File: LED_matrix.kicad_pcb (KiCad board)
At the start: 2 copper layers, 26 x 52 mm, 77 parts, among them J1 Conn_02x20_Odd_Even

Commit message: start adding more dense LED matrix
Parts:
- added D61: LED, custom_LED_footprint:LED_0402_1005Metric, F.Cu at (125.0, 87.9)
- added D62: LED, custom_LED_footprint:LED_0402_1005Metric, F.Cu at (124.9, 89.1)
- added D63: LED, custom_LED_footprint:LED_0402_1005Metric, F.Cu at (125.1, 91.2)
- added D64: LED, custom_LED_footprint:LED_0402_1005Metric, F.Cu at (127.5, 90.8)
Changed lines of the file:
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@@
     (tracks 426)
     (zones 0)
-    (modules 77)
-    (nets 33)
+    (modules 81)
+    (nets 37)
   )
   (page A4)
@@
   (net 31 /c_4)
   (net 32 /c_5)
+  (net 33 "Net-(D61-Pad1)")
+  (net 34 "Net-(D61-Pad2)")
+  (net 35 "Net-(D62-Pad2)")
+  (net 36 "Net-(D63-Pad1)")
   (net_class Default "This is the default net class."
     (clearance 0.18)
@@
     (add_net /row_8)
     (add_net /row_9)
+    (add_net "Net-(D61-Pad1)")
+    (add_net "Net-(D61-Pad2)")
+    (add_net "Net-(D62-Pad2)")
+    (add_net "Net-(D63-Pad1)")
   )
   (module Connector_PinHeader_2.54mm:PinHeader_2x20_P2.54mm_Vertical (layer B.Cu)
@@
     (model ${KISYS3DMOD}/LED_SMD.3dshapes/LED_0402_1005Metric.wrl
       (at (xyz 0 0 0))
+      (scale (xyz 1 1 1))
+      (rotate (xyz 0 0 0))
+    )
+  )
+  (module custom_LED_footprint:LED_0402_1005Metric (layer F.Cu)
+    (at 125 87.9 135)
+    (descr "LED SMD 0402 (1005 Metric), square (rectangular) end terminal, IPC_7351 nominal, (Body size source: http://www.tortai-tech.com/upload/download/2011102023233369053.pdf), generated with kicad-footprint-generator")
+    (tags LED)
+    (attr smd)
+    (fp_text reference D61 (at 0 -1.17 135) (layer F.SilkS)
+      (effects (font (size 1 1) (thickness 0.15)))
+    )
+    (fp_text value LED (at 0 1.17 135) (layer F.Fab)
+      (effects (font (size 1 1) (thickness 0.15)))
+    )
+    (fp_circle (center -1.09 0) (end -1.04 0) (layer F.SilkS) (width 0.1))
+    (fp_line (start -0.5 0.25) (end -0.5 -0.25) (layer F.Fab) (width 0.1))
+    (fp_line (start -0.5 -0.25) (end 0.5 -0.25) (layer F.Fab) (width 0.1))
+    (fp_line (start 0.5 -0.25) (end 0.5 0.25) (layer F.Fab) (width 0.1))
+    (fp_line (start 0.5 0.25) (end -0.5 0.25) (layer F.Fab) (width 0.1))
+    (fp_line (start -0.4 0.25) (end -0.4 -0.25) (layer F.Fab) (width 0.1))
+    (fp_line (start -0.3 0.25) (end -0.3 -0.25) (layer F.Fab) (width 0.1))
+    (fp_line (start -0.93 0.47) (end -0.93 -0.47) (layer F.CrtYd) (width 0.05))
+    (fp_line (start -0.93 -0.47) (end 0.93 -0.47) (layer F.CrtYd) (width 0.05))
+    (fp_line (start 0.93 -0.47) (end 0.93 0.47) (layer F.CrtYd) (width 0.05))
+    (fp_line (start 0.93 0.47) (end -0.93 0.47) (layer F.CrtYd) (width 0.05))
+    (fp_text user %R (at 0 0 135) (layer F.Fab)
+      (effects (font (size 0.25 0.25) (thickness 0.04)))
+    )
+    (pad 1 smd rect (at -0.4 0 135) (size 0.6 0.5) (layers F.Cu F.Paste F.Mask)
+      (net 33 "Net-(D61-Pad1)"))
+    (pad 2 smd rect (at 0.4 0 135) (size 0.6 0.5) (layers F.Cu F.Paste F.Mask)
+      (net 34 "Net-(D61-Pad2)"))
+    (model ${KISYS3DMOD}/LED_SMD.3dshapes/LED_0402_1005Metric.wrl
+      (at (xyz 0 0 0))
+      (scale (xyz 1 1 1))
+      (rotate (xyz 0 0 0))
+    )
+  )
+  (module custom_LED_footprint:LED_0402_1005Metric (layer F.Cu)
+    (at 124.925 89.1 315)
+    (descr "LED SMD 0402 (1005 Metric), square (rectangular) end terminal, IPC_7351 nominal, (Body size source: http://www.tortai-tech.com/upload/download/2011102023233369053.pdf), generated with kicad-footprint-generator")
+    (tags LED)
+    (attr smd)
+    (fp_text reference D62 (at 0 -1.17 315) (layer F.SilkS)
+      (effects (font (size 1 1) (thickness 0.15)))
+    )
+    (fp_text value LED (at 0 1.17 315) (layer F.Fab)
+      (effects (font (size 1 1) (thickness 0.15)))
+    )
+    (fp_circle (center -1.09 0) (end -1.04 0) (layer F.SilkS) (width 0.1))
+    (fp_line (start -0.5 0.25) (end -0.5 -0.25) (layer F.Fab) (width 0.1))
+    (fp_line (start -0.5 -0.25) (end 0.5 -0.25) (layer F.Fab) (width 0.1))
+    (fp_line (start 0.5 -0.25) (end 0.5 0.25) (layer F.Fab) (width 0.1))
+    (fp_line (start 0.5 0.25) (end -0.5 0.25) (layer F.Fab) (width 0.1))
+    (fp_line (start -0.4 0.25) (end -0.4 -0.25) (layer F.Fab) (width 0.1))
+    (fp_line (start -0.3 0.25) (end -0.3 -0.25) (layer F.Fab) (width 0.1))
+    (fp_line (start -0.93 0.47) (end -0.93 -0.47) (layer F.CrtYd) (width 0.05))
+    (fp_line (start -0.93 -0.47) (end 0.93 -0.47) (layer F.CrtYd) (width 0.05))
+    (fp_line (start 0.93 -0.47) (end 0.93 0.47) (layer F.CrtYd) (width 0.05))
+    (fp_line (start 0.93 0.47) (end -0.93 0.47) (layer F.CrtYd) (width 0.05))
+    (fp_text user %R (at 0 0 315) (layer F.Fab)
+      (effects (font (size 0.25 0.25) (thickness 0.04)))
+    )
+    (pad 1 smd rect (at -0.4 0 315) (size 0.6 0.5) (layers F.Cu F.Paste F.Mask)
+      (net 33 "Net-(D61-Pad1)"))
+    (pad 2 smd rect (at 0.4 0 315) (size 0.6 0.5) (layers F.Cu F.Paste F.Mask)
+      (net 35 "Net-(D62-Pad2)"))
+    (model ${KISYS3DMOD}/LED_SMD.3dshapes/LED_0402_1005Metric.wrl
+      (at (xyz 0 0 0))
+      (scale (xyz 1 1 1))
+      (rotate (xyz 0 0 0))
+    )
+  )
+  (module custom_LED_footprint:LED_0402_1005Metric (layer F.Cu)
+    (at 125.1 91.175 135)
+    (descr "LED SMD 0402 (1005 Metric), square (rectangular) end terminal, IPC_7351 nominal, (Body size source: http://www.tortai-tech.com/upload/download/2011102023233369053.pdf), generated with kicad-footprint-generator")
+    (tags LED)
+    (attr smd)
+    (fp_text reference D63 (at 0 -1.17 135) (layer F.SilkS)
+      (effects (font (size 1 1) (thickness 0.15)))
+    )
+    (fp_text value LED (at 0 1.17 135) (layer F.Fab)
+      (effects (font (size 1 1) (thickness 0.15)))
+    )
+    (fp_text user %R (at 0 0 135) (layer F.Fab)
+      (effects (font (size 0.25 0.25) (thickness 0.04)))
+    )
+    (fp_line (start 0.93 0.47) (end -0.93 0.47) (layer F.CrtYd) (width 0.05))
+    (fp_line (start 0.93 -0.47) (end 0.93 0.47) (layer F.CrtYd) (width 0.05))
+    (fp_line (start -0.93 -0.47) (end 0.93 -0.47) (layer F.CrtYd) (width 0.05))
+    (fp_line (start -0.93 0.47) (end -0.93 -0.47) (layer F.CrtYd) (width 0.05))
+    (fp_line (start -0.3 0.25) (end -0.3 -0.25) (layer F.Fab) (width 0.1))
+    (fp_line (start -0.4 0.25) (end -0.4 -0.25) (layer F.Fab) (width 0.1))
+    (fp_line (start 0.5 0.25) (end -0.5 0.25) (layer F.Fab) (width 0.1))
+    (fp_line (start 0.5 -0.25) (end 0.5 0.25) (layer F.Fab) (width 0.1))
+    (fp_line (start -0.5 -0.25) (end 0.5 -0.25) (layer F.Fab) (width 0.1))
+    (fp_line (start -0.5 0.25) (end -0.5 -0.25) (layer F.Fab) (width 0.1))
+    (fp_circle (center -1.09 0) (end -1.04 0) (layer F.SilkS) (width 0.1))
+    (pad 2 smd rect (at 0.4 0 135) (size 0.6 0.5) (layers F.Cu F.Paste F.Mask)
+      (net 34 "Net-(D61-Pad2)"))
+    (pad 1 smd rect (at -0.4 0 135) (size 0.6 0.5) (layers F.Cu F.Paste F.Mask)
+      (net 36 "Net-(D63-Pad1)"))
+    (model ${KISYS3DMOD}/LED_SMD.3dshapes/LED_0402_1005Metric.wrl
+      (at (xyz 0 0 0))
+      (scale (xyz 1 1 1))
+      (rotate (xyz 0 0 0))
+    )
+  )
+  (module custom_LED_footprint:LED_0402_1005Metric (layer F.Cu)
+    (at 127.525 90.85 135)
+    (descr "LED SMD 0402 (1005 Metric), square (rectangular) end terminal, IPC_7351 nominal, (Body size source: http://www.tortai-tech.com/upload/download/2011102023233369053.pdf), generated with kicad-footprint-generator")
+    (tags LED)
+    (attr smd)
+    (fp_text reference D64 (at 0 -1.17 135) (layer F.SilkS)
+      (effects (font (size 1 1) (thickness 0.15)))
+    )
+    (fp_text value LED (at 0 1.17 135) (layer F.Fab)
+      (effects (font (size 1 1) (thickness 0.15)))
+    )
+    (fp_text user %R (at 0 0 135) (layer F.Fab)
+      (effects (font (size 0.25 0.25) (thickness 0.04)))
+    )
+    (fp_line (start 0.93 0.47) (end -0.93 0.47) (layer F.CrtYd) (width 0.05))
+    (fp_line (start 0.93 -0.47) (end 0.93 0.47) (layer F.CrtYd) (width 0.05))
+    (fp_line (start -0.93 -0.47) (end 0.93 -0.47) (layer F.CrtYd) (width 0.05))
+    (fp_line (start -0.93 0.47) (end -0.93 -0.47) (layer F.CrtYd) (width 0.05))
+    (fp_line (start -0.3 0.25) (end -0.3 -0.25) (layer F.Fab) (width 0.1))
+    (fp_line (start -0.4 0.25) (end -0.4 -0.25) (layer F.Fab) (width 0.1))
+    (fp_line (start 0.5 0.25) (end -0.5 0.25) (layer F.Fab) (width 0.1))
+    (fp_line (start 0.5 -0.25) (end 0.5 0.25) (layer F.Fab) (width 0.1))
+    (fp_line (start -0.5 -0.25) (end 0.5 -0.25) (layer F.Fab) (width 0.1))
+    (fp_line (start -0.5 0.25) (end -0.5 -0.25) (layer F.Fab) (width 0.1))
+    (fp_circle (center -1.089999 0) (end -1.04 0) (layer F.SilkS) (width 0.1))
+    (pad 2 smd rect (at 0.4 0 135) (size 0.6 0.5) (layers F.Cu F.Paste F.Mask)
+      (net 35 "Net-(D62-Pad2)"))
+    (pad 1 smd rect (at -0.4 0 135) (size 0.6 0.5) (layers F.Cu F.Paste F.Mask)
+      (net 36 "Net-(D63-Pad1)"))
+    (model ${KISYS3DMOD}/LED_SMD.3dshapes/LED_0402_1005Metric.wrl
+      (at (xyz 0 0 0))

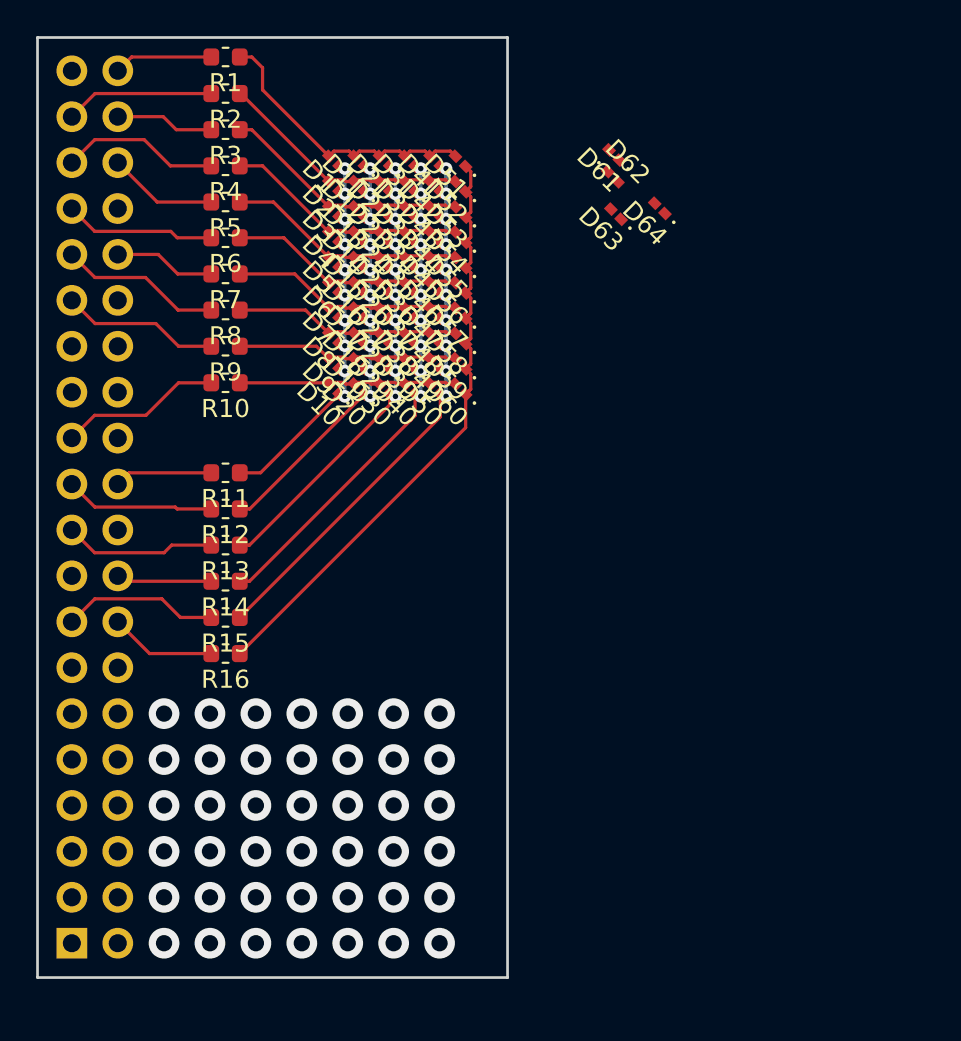
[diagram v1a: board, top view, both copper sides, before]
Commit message: add LED matrix with 1.2mm pitch
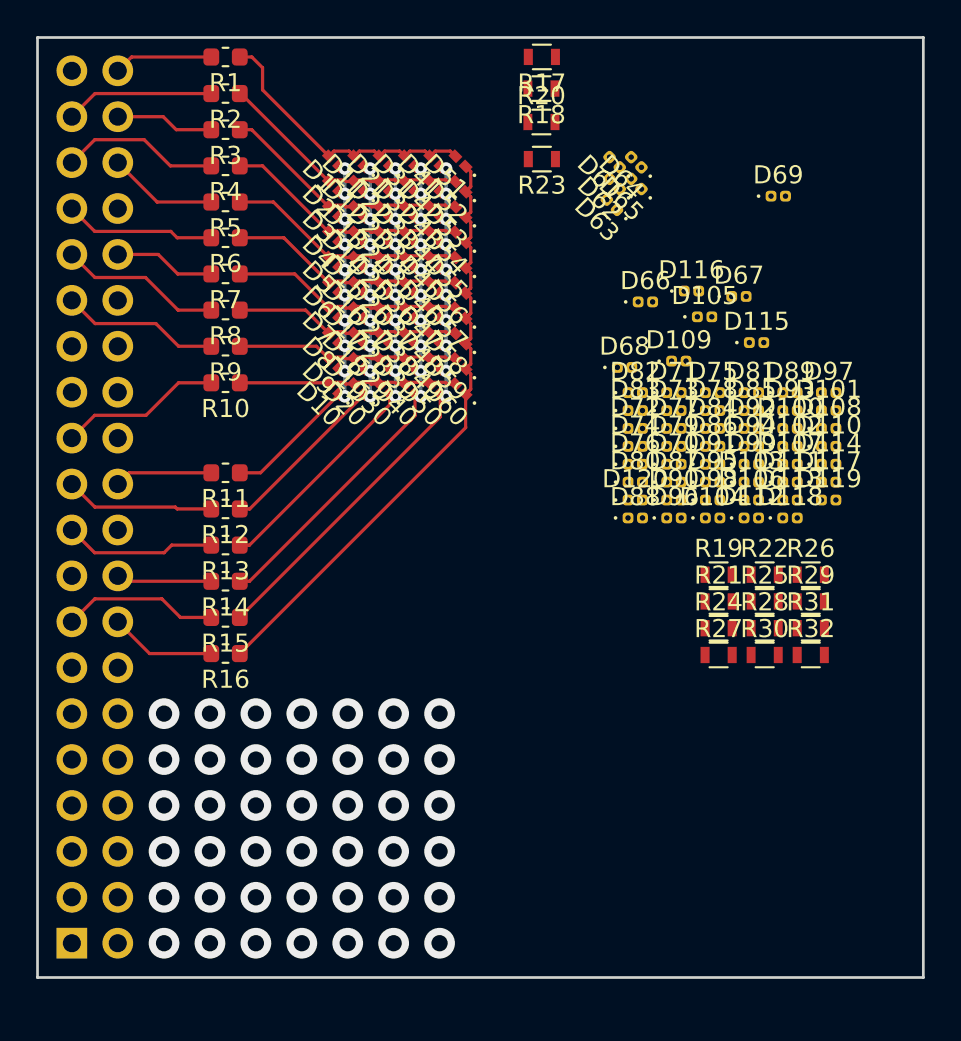
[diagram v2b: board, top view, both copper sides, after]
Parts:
- added D100: LED, custom_LED_footprint:LED_0402_round, F.Cu at (134.7, 103.0)
- added D101: LED, custom_LED_footprint:LED_0402_round, F.Cu at (136.9, 102.0)
- added D102: LED, custom_LED_footprint:LED_0402_round, F.Cu at (134.7, 104.0)
- added D103: LED, custom_LED_footprint:LED_0402_round, F.Cu at (132.6, 106.0)
- added D104: LED, custom_LED_footprint:LED_0402_round, F.Cu at (130.4, 108.0)
- added D105: LED, custom_LED_footprint:LED_0402_round, F.Cu at (130.0, 96.8)
- added D106: LED, custom_LED_footprint:LED_0402_round, F.Cu at (132.6, 107.0)
- added D107: LED, custom_LED_footprint:LED_0402_round, F.Cu at (134.7, 105.0)
- added D108: LED, custom_LED_footprint:LED_0402_round, F.Cu at (136.9, 103.0)
- added D109: LED, custom_LED_footprint:LED_0402_round, F.Cu at (128.6, 99.3)
- added D110: LED, custom_LED_footprint:LED_0402_round, F.Cu at (136.9, 104.0)
- added D111: LED, custom_LED_footprint:LED_0402_round, F.Cu at (134.7, 106.0)
- added D112: LED, custom_LED_footprint:LED_0402_round, F.Cu at (132.6, 108.0)
- added D113: LED, custom_LED_footprint:LED_0402_round, F.Cu at (134.7, 107.0)
- added D114: LED, custom_LED_footprint:LED_0402_round, F.Cu at (136.9, 105.0)
- added D115: LED, custom_LED_footprint:LED_0402_round, F.Cu at (132.9, 98.3)
- added D116: LED, custom_LED_footprint:LED_0402_round, F.Cu at (129.3, 95.4)
- added D117: LED, custom_LED_footprint:LED_0402_round, F.Cu at (136.9, 106.0)
- added D118: LED, custom_LED_footprint:LED_0402_round, F.Cu at (134.7, 108.0)
- added D119: LED, custom_LED_footprint:LED_0402_round, F.Cu at (136.9, 107.0)
- added D120: LED, custom_LED_footprint:LED_0402_round, F.Cu at (126.2, 107.0)
- added D65: LED, custom_LED_footprint:LED_0402_round, F.Cu at (126.2, 89.5)
- added D66: LED, custom_LED_footprint:LED_0402_round, F.Cu at (126.7, 96.0)
- added D67: LED, custom_LED_footprint:LED_0402_round, F.Cu at (131.9, 95.7)
- added D68: LED, custom_LED_footprint:LED_0402_round, F.Cu at (125.6, 99.7)
- added D69: LED, custom_LED_footprint:LED_0402_round, F.Cu at (134.1, 90.2)
- added D70: LED, custom_LED_footprint:LED_0402_round, F.Cu at (128.3, 105.0)
- added D71: LED, custom_LED_footprint:LED_0402_round, F.Cu at (128.3, 101.0)
- added D72: LED, custom_LED_footprint:LED_0402_round, F.Cu at (126.2, 103.0)
- added D73: LED, custom_LED_footprint:LED_0402_round, F.Cu at (128.3, 102.0)
- added D74: LED, custom_LED_footprint:LED_0402_round, F.Cu at (126.2, 104.0)
- added D75: LED, custom_LED_footprint:LED_0402_round, F.Cu at (130.4, 101.0)
- added D76: LED, custom_LED_footprint:LED_0402_round, F.Cu at (126.2, 105.0)
- added D77: LED, custom_LED_footprint:LED_0402_round, F.Cu at (128.3, 103.0)
- added D78: LED, custom_LED_footprint:LED_0402_round, F.Cu at (130.4, 102.0)
- added D79: LED, custom_LED_footprint:LED_0402_round, F.Cu at (128.3, 104.0)
- added D80: LED, custom_LED_footprint:LED_0402_round, F.Cu at (126.2, 106.0)
- added D81: LED, custom_LED_footprint:LED_0402_round, F.Cu at (132.6, 101.0)
- added D82: LED, custom_LED_footprint:LED_0402_round, F.Cu at (126.2, 101.0)
- added D83: LED, custom_LED_footprint:LED_0402_round, F.Cu at (126.2, 102.0)
- added D84: LED, custom_LED_footprint:LED_0402_round, F.Cu at (130.4, 103.0)
- added D85: LED, custom_LED_footprint:LED_0402_round, F.Cu at (132.6, 102.0)
- added D86: LED, custom_LED_footprint:LED_0402_round, F.Cu at (130.4, 104.0)
- added D87: LED, custom_LED_footprint:LED_0402_round, F.Cu at (128.3, 106.0)
- added D88: LED, custom_LED_footprint:LED_0402_round, F.Cu at (126.2, 108.0)
- added D89: LED, custom_LED_footprint:LED_0402_round, F.Cu at (134.7, 101.0)
- added D90: LED, custom_LED_footprint:LED_0402_round, F.Cu at (128.3, 107.0)
- added D91: LED, custom_LED_footprint:LED_0402_round, F.Cu at (130.4, 105.0)
- added D92: LED, custom_LED_footprint:LED_0402_round, F.Cu at (132.6, 103.0)
- added D93: LED, custom_LED_footprint:LED_0402_round, F.Cu at (134.7, 102.0)
- added D94: LED, custom_LED_footprint:LED_0402_round, F.Cu at (132.6, 104.0)
- added D95: LED, custom_LED_footprint:LED_0402_round, F.Cu at (130.4, 106.0)
- added D96: LED, custom_LED_footprint:LED_0402_round, F.Cu at (128.3, 108.0)
- added D97: LED, custom_LED_footprint:LED_0402_round, F.Cu at (136.9, 101.0)
- added D98: LED, custom_LED_footprint:LED_0402_round, F.Cu at (130.4, 107.0)
- added D99: LED, custom_LED_footprint:LED_0402_round, F.Cu at (132.6, 105.0)
- added R17: 100R, Resistors_SMD:R_0603, F.Cu at (121.0, 82.5)
- added R18: 100R, Resistors_SMD:R_0603, F.Cu at (121.0, 84.2)
- added R19: 100R, Resistors_SMD:R_0603, F.Cu at (130.8, 111.1)
- added R20: 100R, Resistors_SMD:R_0603, F.Cu at (121.0, 86.1)
- added R21: 100R, Resistors_SMD:R_0603, F.Cu at (130.8, 112.6)
- added R22: 100R, Resistors_SMD:R_0603, F.Cu at (133.3, 111.1)
- added R23: 100R, Resistors_SMD:R_0603, F.Cu at (121.0, 88.1)
- added R24: 100R, Resistors_SMD:R_0603, F.Cu at (130.8, 114.1)
- added R25: 100R, Resistors_SMD:R_0603, F.Cu at (133.3, 112.6)
- added R26: 100R, Resistors_SMD:R_0603, F.Cu at (135.9, 111.1)
- added R27: 100R, Resistors_SMD:R_0603, F.Cu at (130.8, 115.6)
- added R28: 100R, Resistors_SMD:R_0603, F.Cu at (133.3, 114.1)
- added R29: 100R, Resistors_SMD:R_0603, F.Cu at (135.9, 112.6)
- added R30: 100R, Resistors_SMD:R_0603, F.Cu at (133.3, 115.6)
- added R31: 100R, Resistors_SMD:R_0603, F.Cu at (135.9, 114.1)
- added R32: 100R, Resistors_SMD:R_0603, F.Cu at (135.9, 115.6)
- D61, D62, D63, D64: footprint custom_LED_footprint:LED_0402_1005Metric -> custom_LED_footprint:LED_0402_round
- moved D64 2.86 mm to (126.2, 88.3)
- moved D63 0.57 mm to (124.9, 90.7)
- moved D62 0.41 mm to (125.0, 89.5), turned to 135 degrees
- moved D61 0.40 mm to (125.0, 88.3)
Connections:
- D61 pad 1: Net-(D61-Pad1) -> /c_01
- D61 pad 2: Net-(D61-Pad2) -> /r_01
- D62 pad 1: Net-(D61-Pad1) -> /c_01
- D62 pad 2: Net-(D62-Pad2) -> /r_11
- D63 pad 1: Net-(D63-Pad1) -> /c_01
- D63 pad 2: Net-(D61-Pad2) -> /r_21
- D64 pad 1: Net-(D63-Pad1) -> /c_01
- D64 pad 2: Net-(D62-Pad2) -> /r_31
- J1 pad 1: (no net) -> Net-(J1-Pad1)
- J1 pad 10: (no net) -> Net-(J1-Pad10)
- J1 pad 11: (no net) -> Net-(J1-Pad11)
- J1 pad 12: (no net) -> Net-(J1-Pad12)
- J1 pad 13: (no net) -> Net-(J1-Pad13)
- J1 pad 14: (no net) -> Net-(J1-Pad14)
- J1 pad 17: (no net) -> Net-(J1-Pad17)
- J1 pad 2: (no net) -> Net-(J1-Pad2)
- J1 pad 20: (no net) -> Net-(J1-Pad20)
- J1 pad 24: (no net) -> Net-(J1-Pad24)
- J1 pad 25: (no net) -> Net-(J1-Pad25)
- J1 pad 26: (no net) -> Net-(J1-Pad26)
- J1 pad 27: (no net) -> Net-(J1-Pad27)
- J1 pad 28: (no net) -> Net-(J1-Pad28)
- J1 pad 3: (no net) -> Net-(J1-Pad3)
- J1 pad 30: (no net) -> Net-(J1-Pad30)
- J1 pad 34: (no net) -> Net-(J1-Pad34)
- J1 pad 39: (no net) -> Net-(J1-Pad39)
- J1 pad 4: (no net) -> Net-(J1-Pad4)
- J1 pad 5: (no net) -> Net-(J1-Pad5)
- J1 pad 6: (no net) -> Net-(J1-Pad6)
- J1 pad 7: (no net) -> Net-(J1-Pad7)
- J1 pad 8: (no net) -> Net-(J1-Pad8)
- J1 pad 9: (no net) -> Net-(J1-Pad9)
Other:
- board size 26 x 52 mm -> 49 x 52 mm
- net class Default: clearance 0.18 -> 0.16; trace_width 0.18 -> 0.16; via_dia 0.7 -> 0.6
- rule trace_clearance: 0.18 -> 0.16
- rule trace_min: 0.18 -> 0.16
- rule via_min_size: 0.7 -> 0.6

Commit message: align LEDs
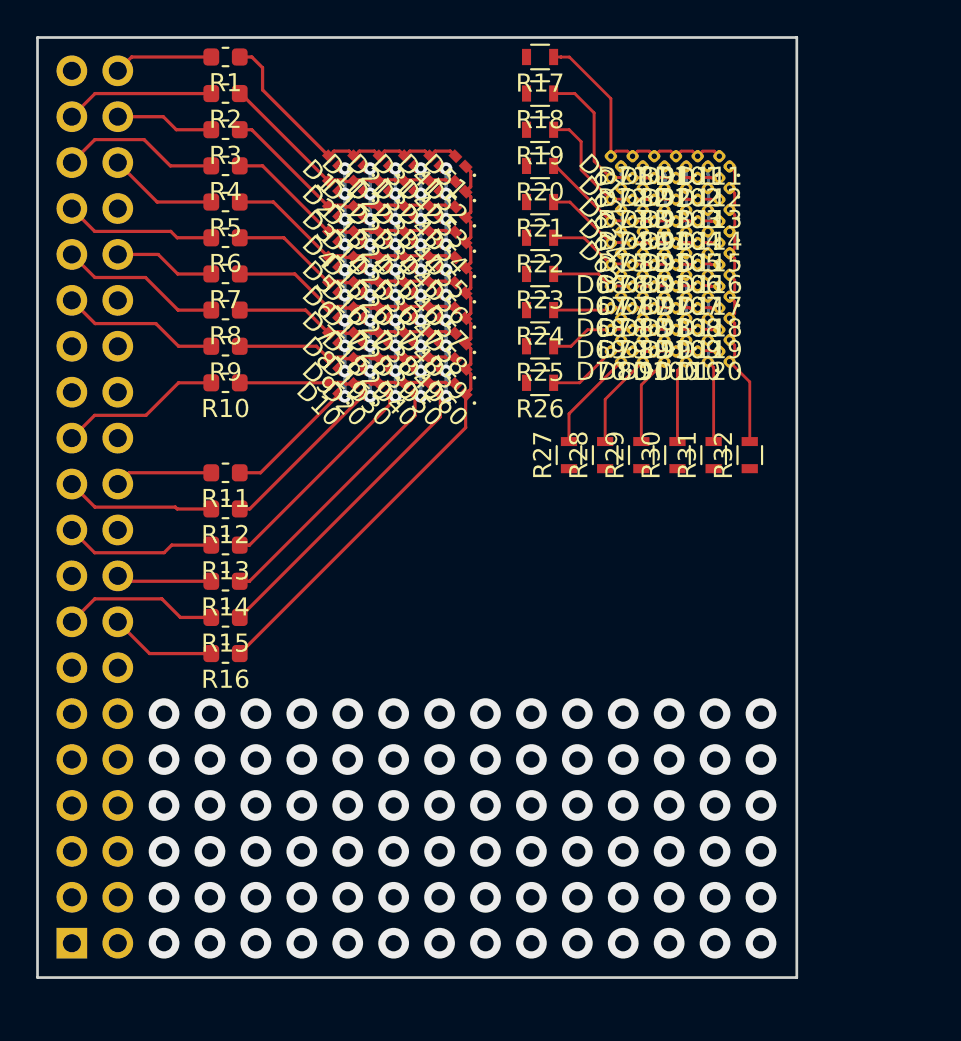
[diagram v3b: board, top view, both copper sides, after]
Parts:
- moved R19 26.5 mm to (120.9, 86.5), turned to 180 degrees
- moved R21 24.2 mm to (120.9, 90.5), turned to 180 degrees
- moved R22 22.4 mm to (120.9, 92.5), turned to 180 degrees
- moved R24 20.2 mm to (120.9, 96.5), turned to 180 degrees
- moved R25 18.8 mm to (120.9, 98.5), turned to 180 degrees
- moved D112 18.6 mm to (131.1, 89.5), turned to 135 degrees
- moved R26 18.4 mm to (120.9, 100.5), turned to 180 degrees
- moved D111 18.1 mm to (131.1, 88.2), turned to 135 degrees
- moved D91 16.8 mm to (128.7, 88.2), turned to 135 degrees
- moved D113 16.7 mm to (131.1, 90.7), turned to 135 degrees
- moved D104 16.1 mm to (129.9, 91.8), turned to 135 degrees
- moved D103 15.6 mm to (129.9, 90.7), turned to 135 degrees
- moved D101 15.4 mm to (129.9, 88.2), turned to 135 degrees
- moved D102 15.3 mm to (129.9, 89.5), turned to 135 degrees
- moved D114 14.4 mm to (131.1, 91.8), turned to 135 degrees
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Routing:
- net /c_51: track 0.00 -> 17.8 mm
- net /c_01: track 0.00 -> 16.4 mm
- net /c_11: track 0.00 -> 16.1 mm
- net /c_21: track 0.00 -> 15.8 mm
- net /c_31: track 0.00 -> 15.4 mm
- net /c_41: track 0.00 -> 15.4 mm
- net /r_01: track 0.00 -> 14.5 mm
- net /r_11: track 0.00 -> 12.8 mm
- net /r_21: track 0.00 -> 11.8 mm
- net /r_31: track 0.00 -> 10.6 mm
- net /r_41: track 0.00 -> 10.2 mm
- net /r_91: track 0.00 -> 10.0 mm
- net /r_51: track 0.00 -> 9.93 mm
- net /r_81: track 0.00 -> 9.65 mm
- net /r_61: track 0.00 -> 9.59 mm
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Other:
- board size 49 x 52 mm -> 42 x 52 mm
